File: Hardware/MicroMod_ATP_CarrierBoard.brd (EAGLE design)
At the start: 86.4 x 55.9 mm, 216 parts, among them J19 QWIIC_RIGHT_ANGLE, J2 JTAG, J20 QWIIC_RIGHT_ANGLE, J21 1X04_SMD_STRAIGHT_COMBO, J4 USB_A_SMT_FEMALE, J6 MICROMOD-2222-C, J8 1X04_SMD_STRAIGHT_COMBO, U5 AP7361C-33

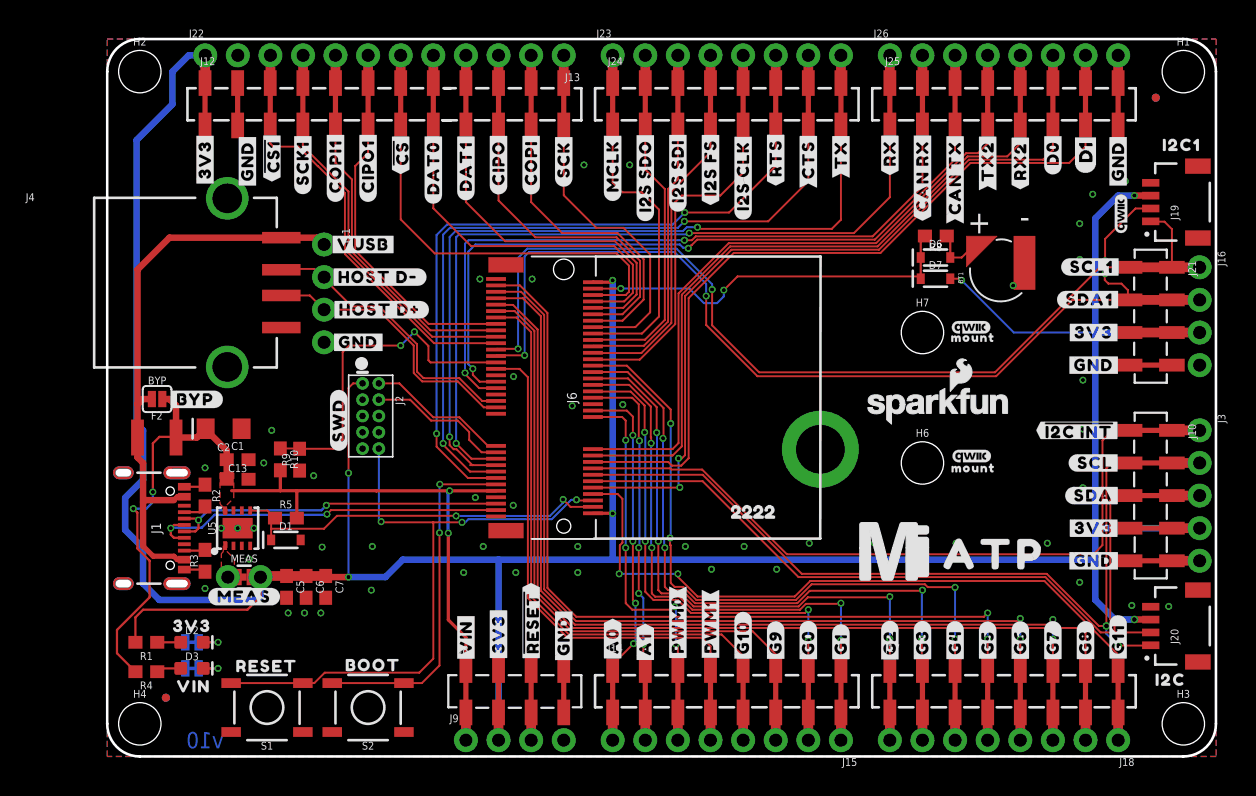
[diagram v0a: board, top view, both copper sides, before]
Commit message: Replaces all connectors with their updated version
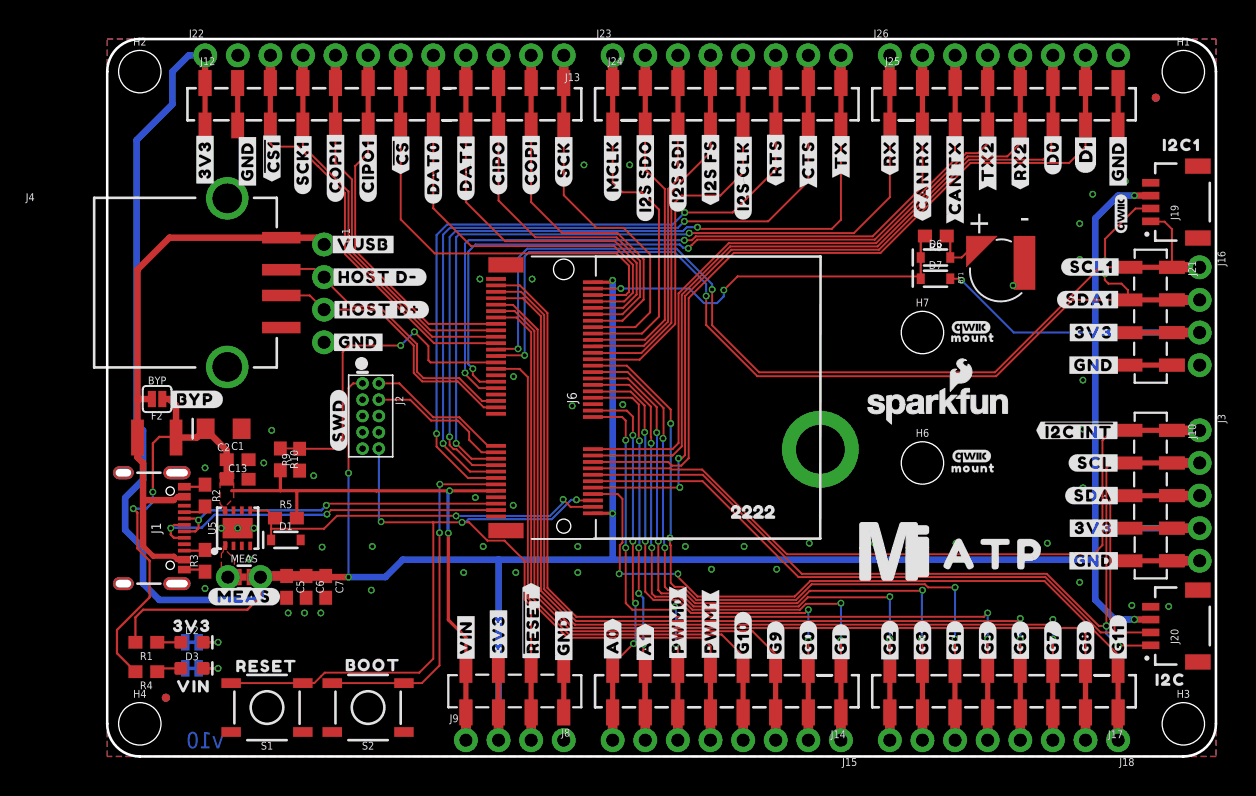
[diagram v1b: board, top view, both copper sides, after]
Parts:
- removed U$84: (no value), fl2:#CIPO#DAT0#5
- J24: device SparkFun-Connectors:1X08_SMD_COMBINED -> testing_header_lib:1X08_SMD_COMBINED
- moved J14 17.8 mm to (57.1, 5.08), turned to 180 degrees
- moved J17 17.8 mm to (78.7, 5.08), turned to 180 degrees
- moved J8 7.62 mm to (35.6, 5.08), turned to 180 degrees
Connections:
- removed net !RESET!: J8.3, J8.3-2, J9.3
- net !CS!/DAT3: no longer J12.7@2
- net !CS1: no longer J12.3@2
- net !RESET: now also J8.2, J9.3
- net 3.3V: now also J8.3; no longer J10.4-2, J12.1@2, J21.3-2, J8.2, J8.2-2
- net A0: now also J14.8; no longer J14.1, J14.1@2
- net A1: now also J14.7; no longer J14.2, J14.2@2
- net CAN_RXI: no longer J25.2@2
- net CAN_TXO: no longer J25.3@2
- net CIPO/DAT0: no longer J12.10@2
- net CIPO1: no longer J12.6@2
- net COPI: no longer J12.11@2
- net COPI1: no longer J12.5@2
- net CTS1: no longer J24.7@2
- net D0: no longer J25.6@2
- net D1: no longer J25.7@2
- net DAT1: no longer J12.9@2
- net DAT2: no longer J12.8@2
- net G0: now also J14.2; no longer J14.7, J14.7@2
- net G1: now also J14.1; no longer J14.8, J14.8@2
- net G10/ADC_P: now also J14.4; no longer J14.5, J14.5@2
- net G11: now also J17.1; no longer J17.8, J17.8@2
- net G2: now also J17.8; no longer J17.1, J17.1@2
- net G3: now also J17.7; no longer J17.2, J17.2@2
- net G4: now also J17.6; no longer J17.3, J17.3@2
- net G5: now also J17.5; no longer J17.4, J17.4@2
- net G6: now also J17.4; no longer J17.5, J17.5@2
- net G7: now also J17.3; no longer J17.6, J17.6@2
- net G8: now also J17.2; no longer J17.7, J17.7@2
- net G9/ADC_N: now also J14.3; no longer J14.6, J14.6@2
- net GND: now also J8.1; no longer J10.5-2, J12.2@2, J21.4-2, J25.8@2, J8.4, J8.4-2
- net I2C_!INT: no longer J10.1-2
- net I2S_CLK: no longer J24.5@2
- net I2S_SDI: no longer J24.3@2
- net I2S_SDO: no longer J24.2@2
- net I2S_WS: no longer J24.4@2
- net MCLK: no longer J24.1@2
- net PWM0: now also J14.6; no longer J14.3, J14.3@2
- net PWM1: now also J14.5; no longer J14.4, J14.4@2
- net RTS1: no longer J24.6@2
- net RX1: no longer J25.1@2
- net RX2: no longer J25.5@2
- net SCK: no longer J12.12@2
- net SCK1: no longer J12.4@2
- net SCL: no longer J10.2-2
- net SCL1: no longer J21.1-2
- net SDA: no longer J10.3-2
- net SDA1: no longer J21.2-2
- net TX1: no longer J24.8@2
- net TX2: no longer J25.4@2
- net VIN: now also J8.4; no longer J8.1, J8.1-2
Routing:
- net !RESET: track 50.7 -> 73.0 mm
- net VIN: track 75.0 -> 81.1 mm
- net I2S_SDO: track 23.9 -> 29.7 mm
- net !CS1: track 30.1 -> 35.8 mm
- net RX2: track 53.5 -> 59.3 mm
- net MCLK: track 24.8 -> 30.6 mm
- net I2S_SDI: track 24.1 -> 29.9 mm
- net DAT1: track 29.4 -> 35.1 mm
- net CTS1: track 57.7 -> 63.5 mm
- net COPI: track 26.2 -> 32.0 mm
- net CAN_TXO: track 57.4 -> 63.2 mm
- net CAN_RXI: track 57.1 -> 62.9 mm
- net !CS!/DAT3: track 33.4 -> 39.2 mm
- net RX1: track 62.2 -> 68.0 mm
- net SCK: track 25.4 -> 31.1 mm
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
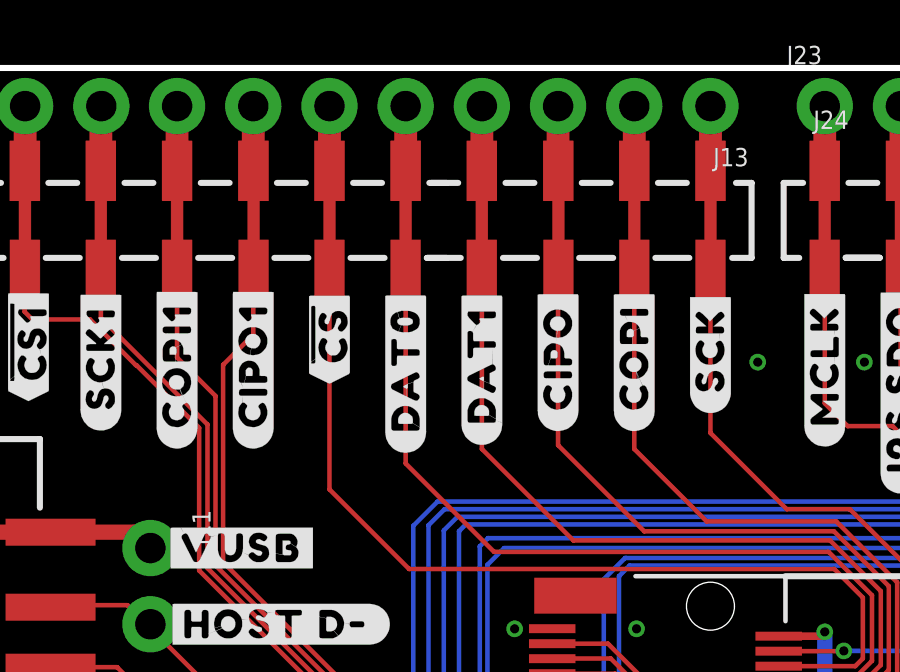
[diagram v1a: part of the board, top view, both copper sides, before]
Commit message: Matches length on the QSPI lines
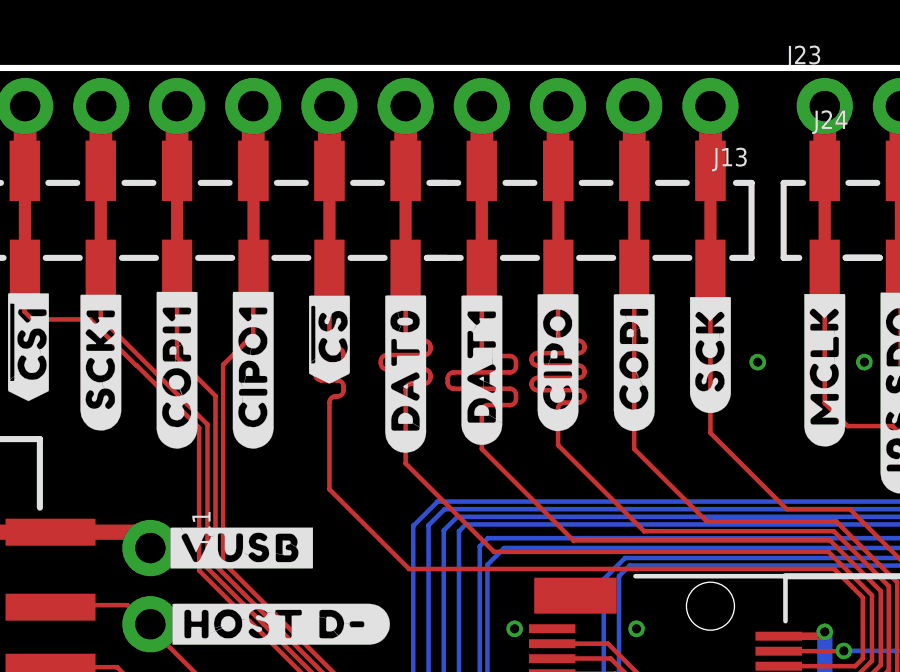
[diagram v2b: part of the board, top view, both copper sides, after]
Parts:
- removed U$48: (no value), fl4:D11
- added U$145: (no value), D1_again:D10
- added U$84: (no value), fl2:#CIPO#DAT0#6
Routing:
- net CIPO/DAT0: track 33.5 -> 40.9 mm
- net DAT1: track 35.1 -> 41.0 mm
- net DAT2: track 37.0 -> 41.0 mm
- net !CS!/DAT3: track 39.2 -> 41.0 mm
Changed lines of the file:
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@@
 <element name="U$88" library="fl3" package="#3V3#1" value="" x="7.62" y="51.943" smashed="yes" rot="MR270"/>
 <element name="U$28" library="headtop" package="#SCK#2" value="" x="35.56" y="46.482" smashed="yes" rot="R90"/>
-<element name="U$48" library="fl4" package="D11" value="" x="76.2" y="52.705" smashed="yes" rot="MR270"/>
 <element name="U$3" library="power" package="#GND#0" value="" x="76.835" y="15.24" smashed="yes"/>
 <element name="U$58" library="power" package="#GND#0" value="" x="78.74" y="46.355" smashed="yes" rot="R90"/>
@@
 <element name="U$143" library="headtop" package="MOUNT10" value="" x="67.31" y="32.639" smashed="yes" rot="MR0"/>
 <element name="U$144" library="SparkFun-MicroMod" package="MICROMOD_LOGO_1" value="" x="36.449" y="28.321" smashed="yes" rot="MR0"/>
+<element name="U$84" library="fl2" package="#CIPO#DAT0#6" value="" x="30.48" y="49.149" smashed="yes" rot="MR270"/>
+<element name="U$145" library="D1_again" package="D10" value="" x="76.2" y="54.356" smashed="yes" rot="MR270"/>
 </elements>
 <signals>
@@
 <wire x1="30.988" y1="40.132" x2="27.94" y2="43.18" width="0.1524" layer="1"/>
 <wire x1="27.94" y1="52.07" x2="27.94" y2="54.61" width="0.762" layer="1"/>
-<wire x1="27.94" y1="43.18" x2="27.94" y2="52.07" width="0.1524" layer="1"/>
+<wire x1="27.94" y1="43.18" x2="27.94" y2="44.43925" width="0.1524" layer="1"/>
+<wire x1="27.94" y1="44.43925" x2="28.1432" y2="44.64245" width="0.1524" layer="1" curve="-90"/>
+<wire x1="28.1432" y1="44.64245" x2="28.8748875" y2="44.64245" width="0.1524" layer="1"/>
+<wire x1="28.8748875" y1="44.64245" x2="29.0780875" y2="44.84565" width="0.1524" layer="1" curve="90"/>
+<wire x1="29.0780875" y1="44.84565" x2="29.0780875" y2="44.9847" width="0.1524" layer="1"/>
+<wire x1="29.0780875" y1="44.9847" x2="28.8748875" y2="45.1879" width="0.1524" layer="1" curve="90"/>
+<wire x1="28.8748875" y1="45.1879" x2="27.0051125" y2="45.1879" width="0.1524" layer="1"/>
+<wire x1="27.0051125" y1="45.1879" x2="26.8019125" y2="45.3911" width="0.1524" layer="1" curve="-90"/>
+<wire x1="26.8019125" y1="45.3911" x2="26.8019125" y2="45.53015" width="0.1524" layer="1"/>
+<wire x1="26.8019125" y1="45.53015" x2="27.0051125" y2="45.73335" width="0.1524" layer="1" curve="-90"/>
+<wire x1="27.0051125" y1="45.73335" x2="28.8748875" y2="45.73335" width="0.1524" layer="1"/>
+<wire x1="28.8748875" y1="45.73335" x2="29.0780875" y2="45.93655" width="0.1524" layer="1" curve="90"/>
+<wire x1="29.0780875" y1="45.93655" x2="29.0780875" y2="46.0756" width="0.1524" layer="1"/>
+<wire x1="29.0780875" y1="46.0756" x2="28.8748875" y2="46.2788" width="0.1524" layer="1" curve="90"/>
+<wire x1="28.8748875" y1="46.2788" x2="28.1432" y2="46.2788" width="0.1524" layer="1"/>
+<wire x1="28.1432" y1="46.2788" x2="27.94" y2="46.482" width="0.1524" layer="1" curve="-90"/>
+<wire x1="27.94" y1="46.482" x2="27.94" y2="52.07" width="0.1524" layer="1"/>
 <wire x1="27.94" y1="52.45" x2="27.94" y2="54.61" width="0.1524" layer="1"/>
 </signal>
@@
 <wire x1="25.5143" y1="39.1795" x2="22.86" y2="41.8338" width="0.1524" layer="1"/>
 <wire x1="22.86" y1="52.07" x2="22.86" y2="54.61" width="0.762" layer="1"/>
-<wire x1="22.86" y1="41.8338" x2="22.86" y2="52.07" width="0.1524" layer="1"/>
+<wire x1="22.86" y1="41.8338" x2="22.86" y2="44.7318125" width="0.1524" layer="1"/>
+<wire x1="22.86" y1="44.7318125" x2="23.0632" y2="44.9350125" width="0.1524" layer="1" curve="-90"/>
+<wire x1="23.0632" y1="44.9350125" x2="23.12695" y2="44.9350125" width="0.1524" layer="1"/>
+<wire x1="23.12695" y1="44.9350125" x2="23.33015" y2="45.1382125" width="0.1524" layer="1" curve="90"/>
+<wire x1="23.33015" y1="45.1382125" x2="23.33015" y2="45.264409375" width="0.1524" layer="1"/>
+<wire x1="23.33015" y1="45.264409375" x2="23.12695" y2="45.467609375" width="0.1524" layer="1" curve="90"/>
+<wire x1="23.12695" y1="45.467609375" x2="22.59305" y2="45.467609375" width="0.1524" layer="1"/>
+<wire x1="22.59305" y1="45.467609375" x2="22.38985" y2="45.670809375" width="0.1524" layer="1" curve="-90"/>
+<wire x1="22.38985" y1="45.670809375" x2="22.38985" y2="45.797003125" width="0.1524" layer="1"/>
+<wire x1="22.38985" y1="45.797003125" x2="22.59305" y2="46.000203125" width="0.1524" layer="1" curve="-90"/>
+<wire x1="22.59305" y1="46.000203125" x2="23.12695" y2="46.000203125" width="0.1524" layer="1"/>
+<wire x1="23.12695" y1="46.000203125" x2="23.33015" y2="46.203403125" width="0.1524" layer="1" curve="90"/>
+<wire x1="23.33015" y1="46.203403125" x2="23.33015" y2="46.3296" width="0.1524" layer="1"/>
+<wire x1="23.33015" y1="46.3296" x2="23.12695" y2="46.5328" width="0.1524" layer="1" curve="90"/>
+<wire x1="23.12695" y1="46.5328" x2="23.0632" y2="46.5328" width="0.1524" layer="1"/>
+<wire x1="23.0632" y1="46.5328" x2="22.86" y2="46.736" width="0.1524" layer="1" curve="-90"/>
+<wire x1="22.86" y1="46.736" x2="22.86" y2="52.07" width="0.1524" layer="1"/>
 <wire x1="22.86" y1="52.45" x2="22.86" y2="54.61" width="0.1524" layer="1"/>
 </signal>
@@
 <wire x1="28.3464" y1="39.751" x2="25.4" y2="42.6974" width="0.1524" layer="1"/>
 <wire x1="25.4" y1="52.07" x2="25.4" y2="54.61" width="0.762" layer="1"/>
-<wire x1="25.4" y1="42.6974" x2="25.4" y2="52.07" width="0.1524" layer="1"/>
+<wire x1="25.4" y1="42.6974" x2="25.4" y2="45.155346875" width="0.1524" layer="1"/>
+<wire x1="25.4" y1="45.155346875" x2="25.6032" y2="45.358546875" width="0.1524" layer="1" curve="-90"/>
+<wire x1="25.6032" y1="45.358546875" x2="26.0236" y2="45.358546875" width="0.1524" layer="1"/>
+<wire x1="26.0236" y1="45.358546875" x2="26.2268" y2="45.561746875" width="0.1524" layer="1" curve="90"/>
+<wire x1="26.2268" y1="45.561746875" x2="26.2268" y2="45.63143125" width="0.1524" layer="1"/>
+<wire x1="26.2268" y1="45.63143125" x2="26.0236" y2="45.83463125" width="0.1524" layer="1" curve="90"/>
+<wire x1="26.0236" y1="45.83463125" x2="24.7764" y2="45.83463125" width="0.1524" layer="1"/>
+<wire x1="24.7764" y1="45.83463125" x2="24.5732" y2="46.03783125" width="0.1524" layer="1" curve="-90"/>
+<wire x1="24.5732" y1="46.03783125" x2="24.5732" y2="46.107515625" width="0.1524" layer="1"/>
+<wire x1="24.5732" y1="46.107515625" x2="24.7764" y2="46.310715625" width="0.1524" layer="1" curve="-90"/>
+<wire x1="24.7764" y1="46.310715625" x2="26.0236" y2="46.310715625" width="0.1524" layer="1"/>
+<wire x1="26.0236" y1="46.310715625" x2="26.2268" y2="46.513915625" width="0.1524" layer="1" curve="90"/>
+<wire x1="26.2268" y1="46.513915625" x2="26.2268" y2="46.5836" width="0.1524" layer="1"/>
+<wire x1="26.2268" y1="46.5836" x2="26.0236" y2="46.7868" width="0.1524" layer="1" curve="90"/>
+<wire x1="26.0236" y1="46.7868" x2="25.6032" y2="46.7868" width="0.1524" layer="1"/>
+<wire x1="25.6032" y1="46.7868" x2="25.4" y2="46.99" width="0.1524" layer="1" curve="-90"/>
+<wire x1="25.4" y1="46.99" x2="25.4" y2="52.07" width="0.1524" layer="1"/>
 <wire x1="25.4" y1="52.452" x2="25.4" y2="54.61" width="0.1524" layer="1"/>
 </signal>
@@
 <wire x1="33.3502" y1="40.4368" x2="30.48" y2="43.307" width="0.1524" layer="1"/>
 <wire x1="30.48" y1="52.07" x2="30.48" y2="54.61" width="0.762" layer="1"/>
-<wire x1="30.48" y1="43.307" x2="30.48" y2="52.07" width="0.1524" layer="1"/>
+<wire x1="30.48" y1="43.307" x2="30.48" y2="44.521878125" width="0.1524" layer="1"/>
+<wire x1="30.48" y1="44.521878125" x2="30.6832" y2="44.725078125" width="0.1524" layer="1" curve="-90"/>
+<wire x1="30.6832" y1="44.725078125" x2="31.162584375" y2="44.725078125" width="0.1524" layer="1"/>
+<wire x1="31.162584375" y1="44.725078125" x2="31.365784375" y2="44.928278125" width="0.1524" layer="1" curve="90"/>
+<wire x1="31.365784375" y1="44.928278125" x2="31.365784375" y2="44.934221875" width="0.1524" layer="1"/>
+<wire x1="31.365784375" y1="44.934221875" x2="31.162584375" y2="45.137421875" width="0.1524" layer="1" curve="90"/>
+<wire x1="31.162584375" y1="45.137421875" x2="29.797415625" y2="45.137421875" width="0.1524" layer="1"/>
+<wire x1="29.797415625" y1="45.137421875" x2="29.594215625" y2="45.340621875" width="0.1524" layer="1" curve="-90"/>
+<wire x1="29.594215625" y1="45.340621875" x2="29.594215625" y2="45.346565625" width="0.1524" layer="1"/>
+<wire x1="29.594215625" y1="45.346565625" x2="29.797415625" y2="45.549765625" width="0.1524" layer="1" curve="-90"/>
+<wire x1="29.797415625" y1="45.549765625" x2="31.162584375" y2="45.549765625" width="0.1524" layer="1"/>
+<wire x1="31.162584375" y1="45.549765625" x2="31.365784375" y2="45.752965625" width="0.1524" layer="1" curve="90"/>
+<wire x1="31.365784375" y1="45.752965625" x2="31.365784375" y2="45.7589125" width="0.1524" layer="1"/>
+<wire x1="31.365784375" y1="45.7589125" x2="31.162584375" y2="45.9621125" width="0.1524" layer="1" curve="90"/>
+<wire x1="31.162584375" y1="45.9621125" x2="29.797415625" y2="45.9621125" width="0.1524" layer="1"/>
+<wire x1="29.797415625" y1="45.9621125" x2="29.594215625" y2="46.1653125" width="0.1524" layer="1" curve="-90"/>
+<wire x1="29.594215625" y1="46.1653125" x2="29.594215625" y2="46.17125625" width="0.1524" layer="1"/>
+<wire x1="29.594215625" y1="46.17125625" x2="29.797415625" y2="46.37445625" width="0.1524" layer="1" curve="-90"/>
+<wire x1="29.797415625" y1="46.37445625" x2="31.162584375" y2="46.37445625" width="0.1524" layer="1"/>
+<wire x1="31.162584375" y1="46.37445625" x2="31.365784375" y2="46.57765625" width="0.1524" layer="1" curve="90"/>
+<wire x1="31.365784375" y1="46.57765625" x2="31.365784375" y2="46.5836" width="0.1524" layer="1"/>
+<wire x1="31.365784375" y1="46.5836" x2="31.162584375" y2="46.7868" width="0.1524" layer="1" curve="90"/>
+<wire x1="31.162584375" y1="46.7868" x2="30.6832" y2="46.7868" width="0.1524" layer="1"/>
+<wire x1="30.6832" y1="46.7868" x2="30.48" y2="46.99" width="0.1524" layer="1" curve="-90"/>
+<wire x1="30.48" y1="46.99" x2="30.48" y2="52.07" width="0.1524" layer="1"/>
 <wire x1="30.48" y1="52.452" x2="30.48" y2="54.61" width="0.1524" layer="1"/>
 </signal>

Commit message: Swaps one 8 pin header in the test lib to on from the main Sparkfun lib
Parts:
- J24: device testing_header_lib:1X08_SMD_COMBINED -> SparkFun-Connectors:1X08_SMD_COMBINED
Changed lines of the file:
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@@
 <attribute name="VALUE" x="77.851" y="38.608" size="0.6096" layer="27" font="vector" ratio="20" rot="R270"/>
 </element>
-<element name="J24" library="testing_header_lib" package="1X08_SMD_COMBINED" value="" x="39.37" y="50.8" smashed="yes">
+<element name="J24" library="SparkFun-Connectors" package="1X08_SMD_COMBINED" value="" x="39.37" y="50.8" smashed="yes">
 <attribute name="NAME" x="38.989" y="53.848" size="0.6096" layer="25" font="vector" ratio="20"/>
 <attribute name="PROD_ID" value="CONN-10204" x="39.37" y="50.8" size="1.778" layer="27" font="vector" ratio="15" display="off"/>
